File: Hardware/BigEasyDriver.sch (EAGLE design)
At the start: 52 parts, among them IC1 A4983ALT1, IC2 LM317L

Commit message: Started v15 revisions
Changed caps and resis to 0603, updated version number on PCB and
Schematic, re-routed a few traces.  Nowhere near done
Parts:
- C1, C10, C11, C2, C6, C7, C8, C9: device SparkFun:CAP0402-CAP -> SparkFun:CAP0603-CAP
- R1, R10, R11, R12, R13, R2, R20, R3, R4, R5, R6, R7, R8, R9: device SparkFun:RESISTOR0402-RES -> SparkFun:RESISTOR0603-RES
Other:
- note added: "v15"

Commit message: Changed Schematic Nets
Nets changed to new specifications
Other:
- note added: "Revised by Patrick Alberts"
- moved on the sheet: JP10, JP14, JP3, JP6

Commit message: Revert "Changed Schematic Nets"
This reverts commit ceb7b9bd87dc9e1a8942882cf4505f035ac33b39.
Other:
- note removed: "Revised by Patrick Alberts"
- moved on the sheet: JP10, JP14, JP3, JP6

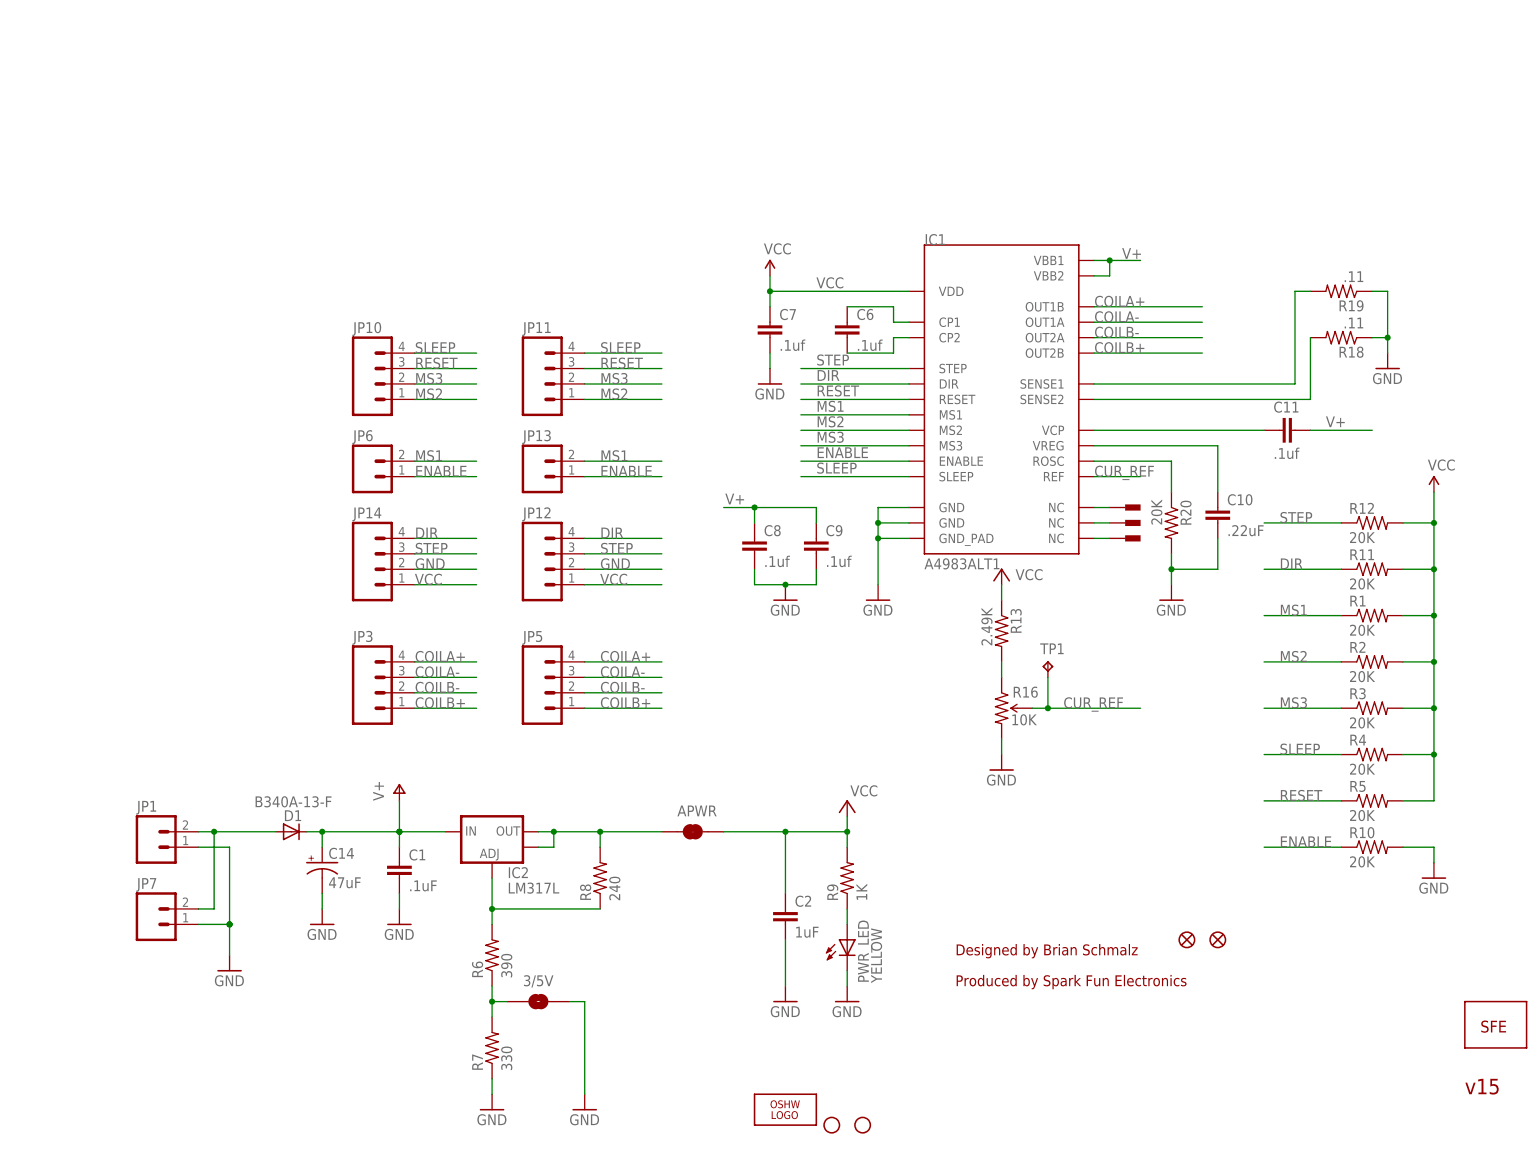
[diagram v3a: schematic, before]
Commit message: Updated Schematic
Changed the nets, the previous commit did not sync correctly.
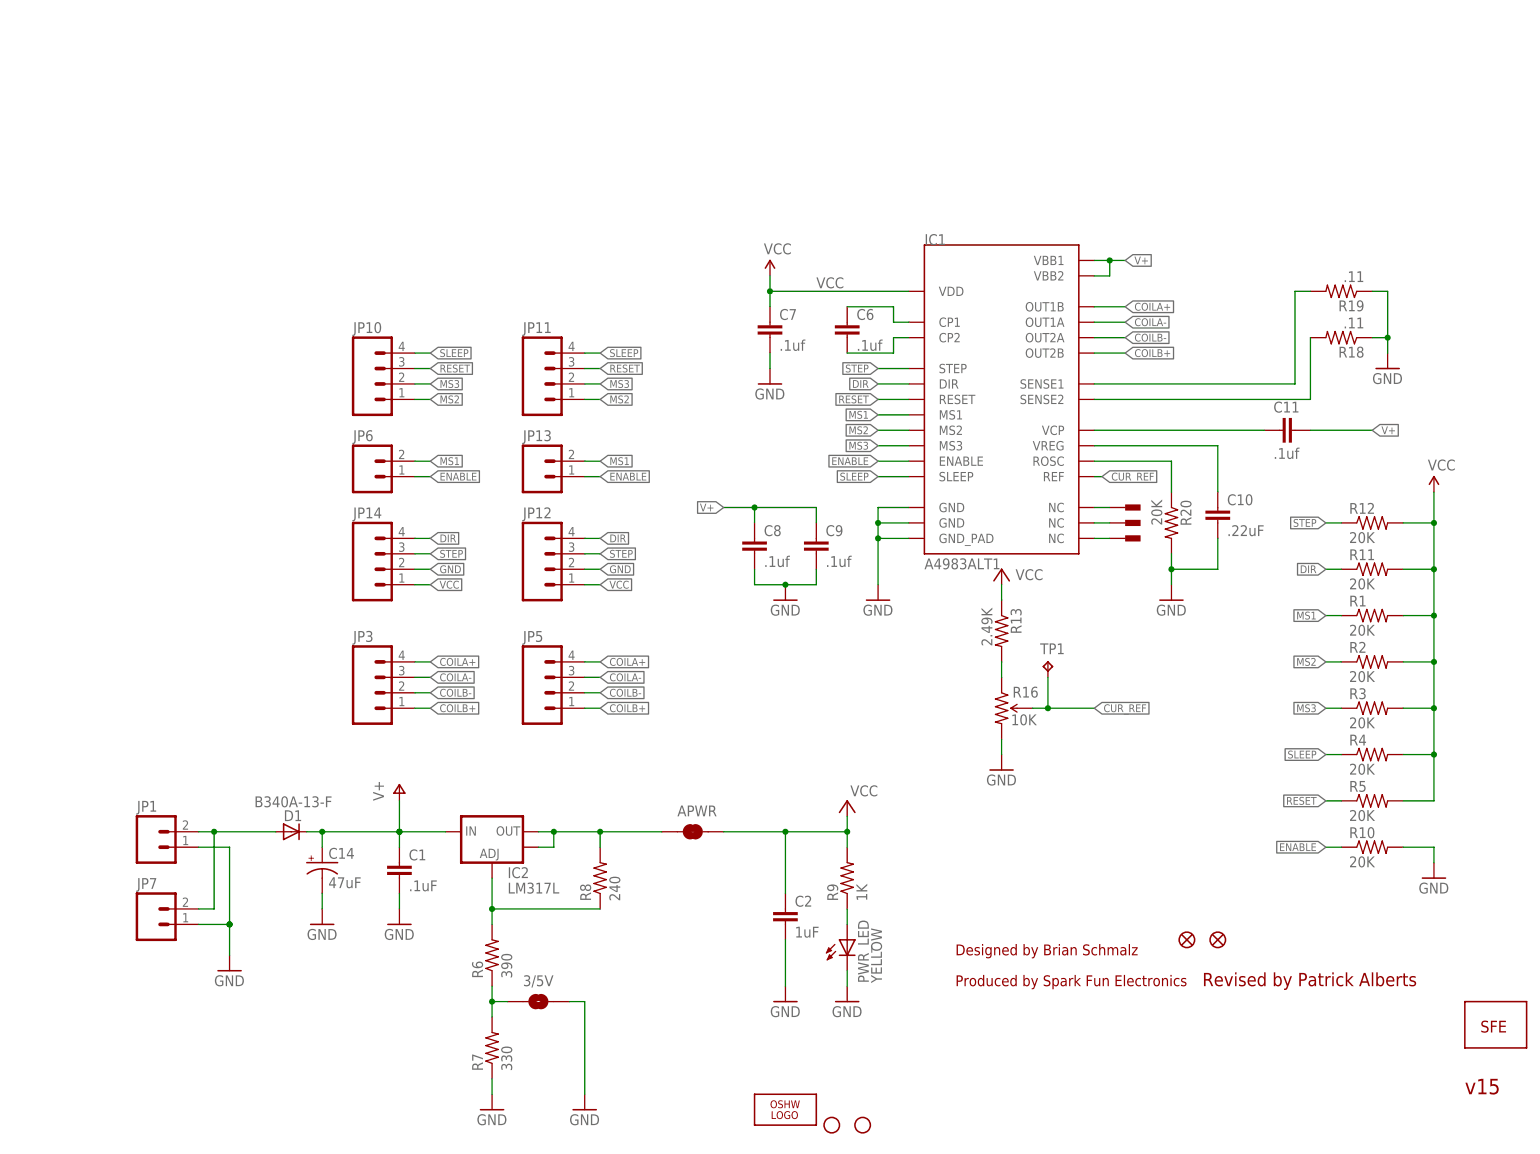
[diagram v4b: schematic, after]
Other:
- note added: "Revised by Patrick Alberts"

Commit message: Frame updated, Angles , Creative Commons added
Added new schematic framrs, cleaned up some trace angels and added the
creative commons license.
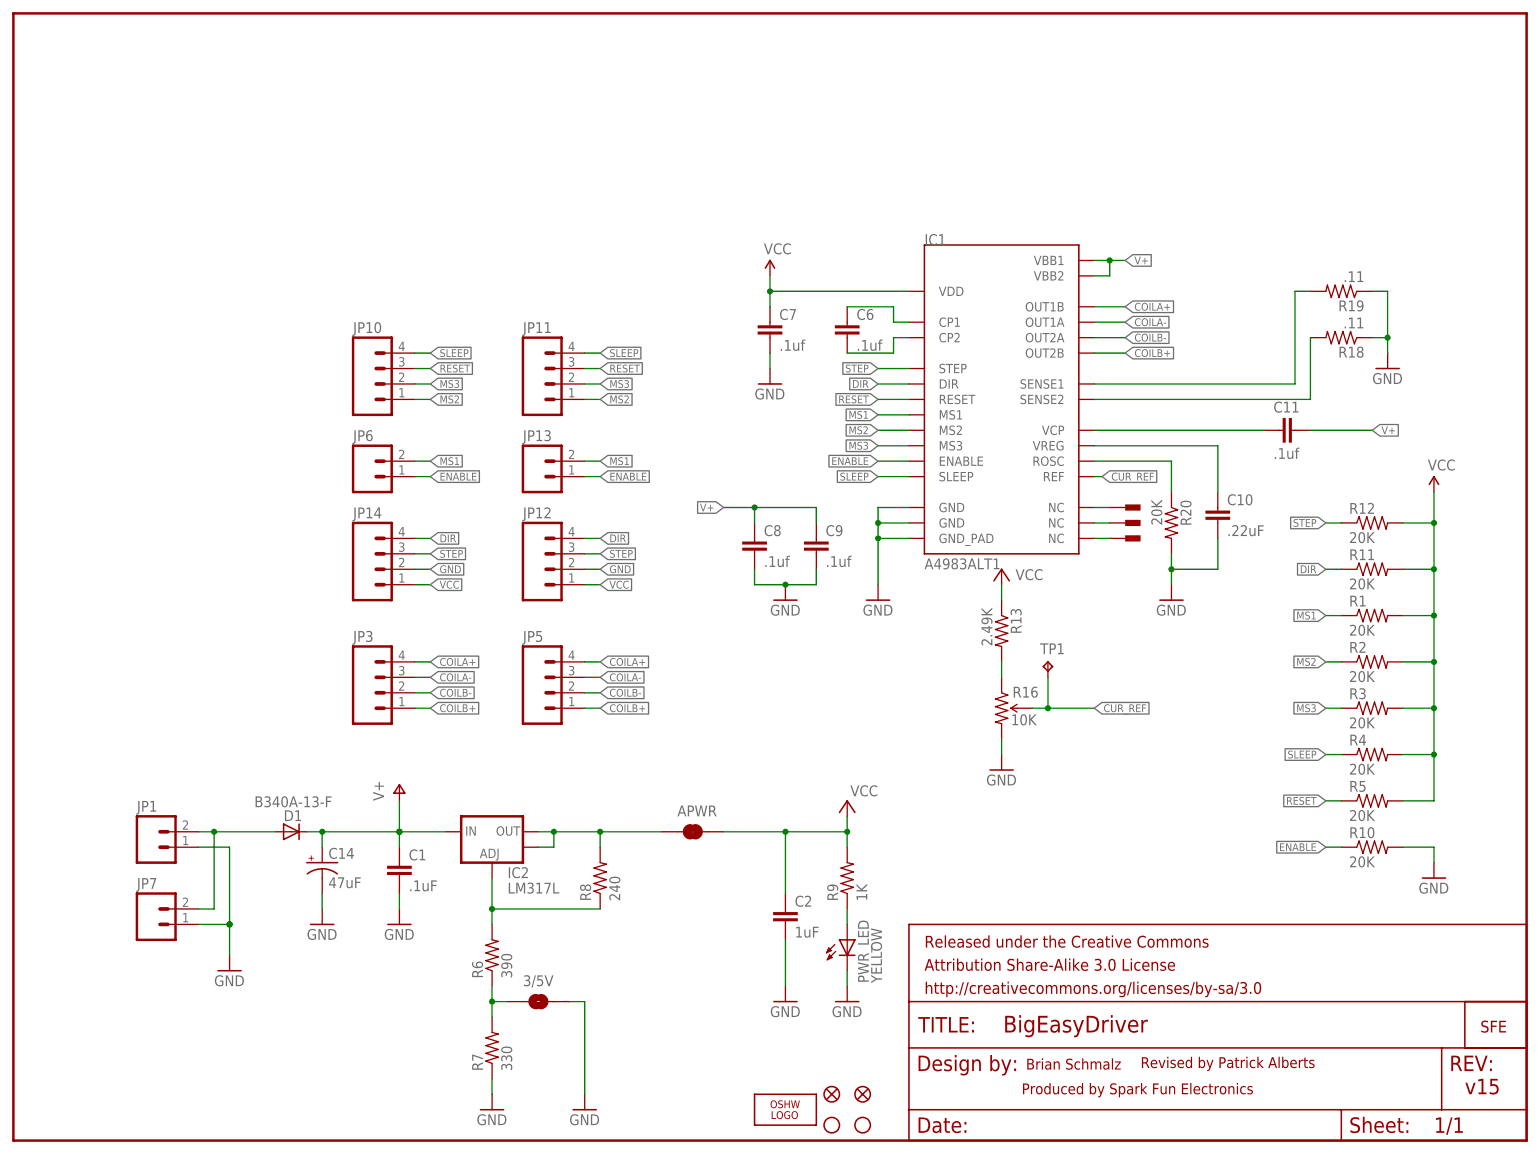
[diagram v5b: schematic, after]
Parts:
- added FRAME1: FRAME-LETTER, SparkFun-Aesthetics:FRAME-LETTER
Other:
- note added: "Brian Schmalz"
- note removed: "Designed by Brian Schmalz"
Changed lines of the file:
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@@
 <layer number="144" name="DrillLegend" color="7" fill="1" visible="no" active="yes"/>
 <layer number="151" name="HeatSink" color="7" fill="1" visible="yes" active="yes"/>
+<layer number="199" name="Contour" color="7" fill="1" visible="no" active="yes"/>
 <layer number="200" name="200bmp" color="1" fill="10" visible="no" active="no"/>
 <layer number="201" name="201bmp" color="2" fill="1" visible="no" active="no"/>
@@
 <part name="MOT_PWR" library="supply1" deviceset="V+" device=""/>
 <part name="GND1" library="supply1" deviceset="GND" device=""/>
-<part name="FRAME1" library="SparkFun" deviceset="FRAME-LETTER" device=""/>
+<part name="FRAME1" library="SparkFun-Aesthetics" deviceset="FRAME-LETTER" device=""/>
 <part name="R6" library="SparkFun" deviceset="RESISTOR" device="0603-RES" value="390"/>
 <part name="R8" library="SparkFun" deviceset="RESISTOR" device="0603-RES" value="240"/>
@@
 <wire x1="12.7" y1="30.48" x2="12.7" y2="55.88" width="0.1524" layer="98" style="shortdash"/>
 <wire x1="111.252" y1="50.8" x2="112.268" y2="50.8" width="0.1524" layer="94"/>
-<text x="154.94" y="30.48" size="1.778" layer="94">Designed by Brian Schmalz</text>
-<text x="154.94" y="25.4" size="1.778" layer="94">Produced by Spark Fun Electronics</text>
+<text x="165.862" y="11.684" size="1.778" layer="94"> Brian Schmalz</text>
+<text x="165.862" y="7.62" size="1.778" layer="94">Produced by Spark Fun Electronics</text>
 <text x="142.24" y="53.34" size="1.778" layer="98">Voltage regulator can supply 100mA</text>
 <text x="71.12" y="58.42" size="1.778" layer="98">Must use LM317</text>
@@
 <text x="2.54" y="2.54" size="1.778" layer="98">-moved vias and retraced as necessary on VCC and TOP layers</text>
 <text x="238.76" y="7.62" size="2.54" layer="94" font="vector">v15</text>
-<text x="195.58" y="25.4" size="2.1844" layer="94" font="vector">Revised by Patrick Alberts</text>
+<text x="185.42" y="11.938" size="1.778" layer="94">Revised by Patrick Alberts</text>
 </plain>
 <instances>
@@
 <instance part="C2" gate="G$1" x="127" y="35.56"/>
 <instance part="LOGO1" gate="G$1" x="127" y="5.08"/>
-<instance part="JP2" gate="G$1" x="193.04" y="33.02"/>
-<instance part="JP4" gate="G$1" x="198.12" y="33.02"/>
+<instance part="JP2" gate="G$1" x="139.7" y="7.62"/>
+<instance part="JP4" gate="G$1" x="134.62" y="7.62"/>
 <instance part="U$3" gate="G$1" x="185.42" y="104.14"/>
 <instance part="U$4" gate="G$1" x="185.42" y="101.6"/>
@@
 <wire x1="124.46" y1="142.24" x2="124.46" y2="139.7" width="0.1524" layer="91"/>
 <junction x="124.46" y="139.7"/>
-<label x="132.08" y="140.208" size="1.778" layer="95"/>
 <pinref part="IC1" gate="G$1" pin="VDD"/>
 <pinref part="C7" gate="G$1" pin="1"/>

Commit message: Version 1.6 update -
* Removed large hole on bottom solder mask (because vias will short out with plane if a metal heatsink is used, this is kinda pointless)
* Changed R13 to 8.3K to give much more useful range of pot motion
* Added current limiting resistors to STEP and DIR lines
* got rid of all angle errors in DRC
* Added more explanation of R16 current adjust pot behavior in schematic
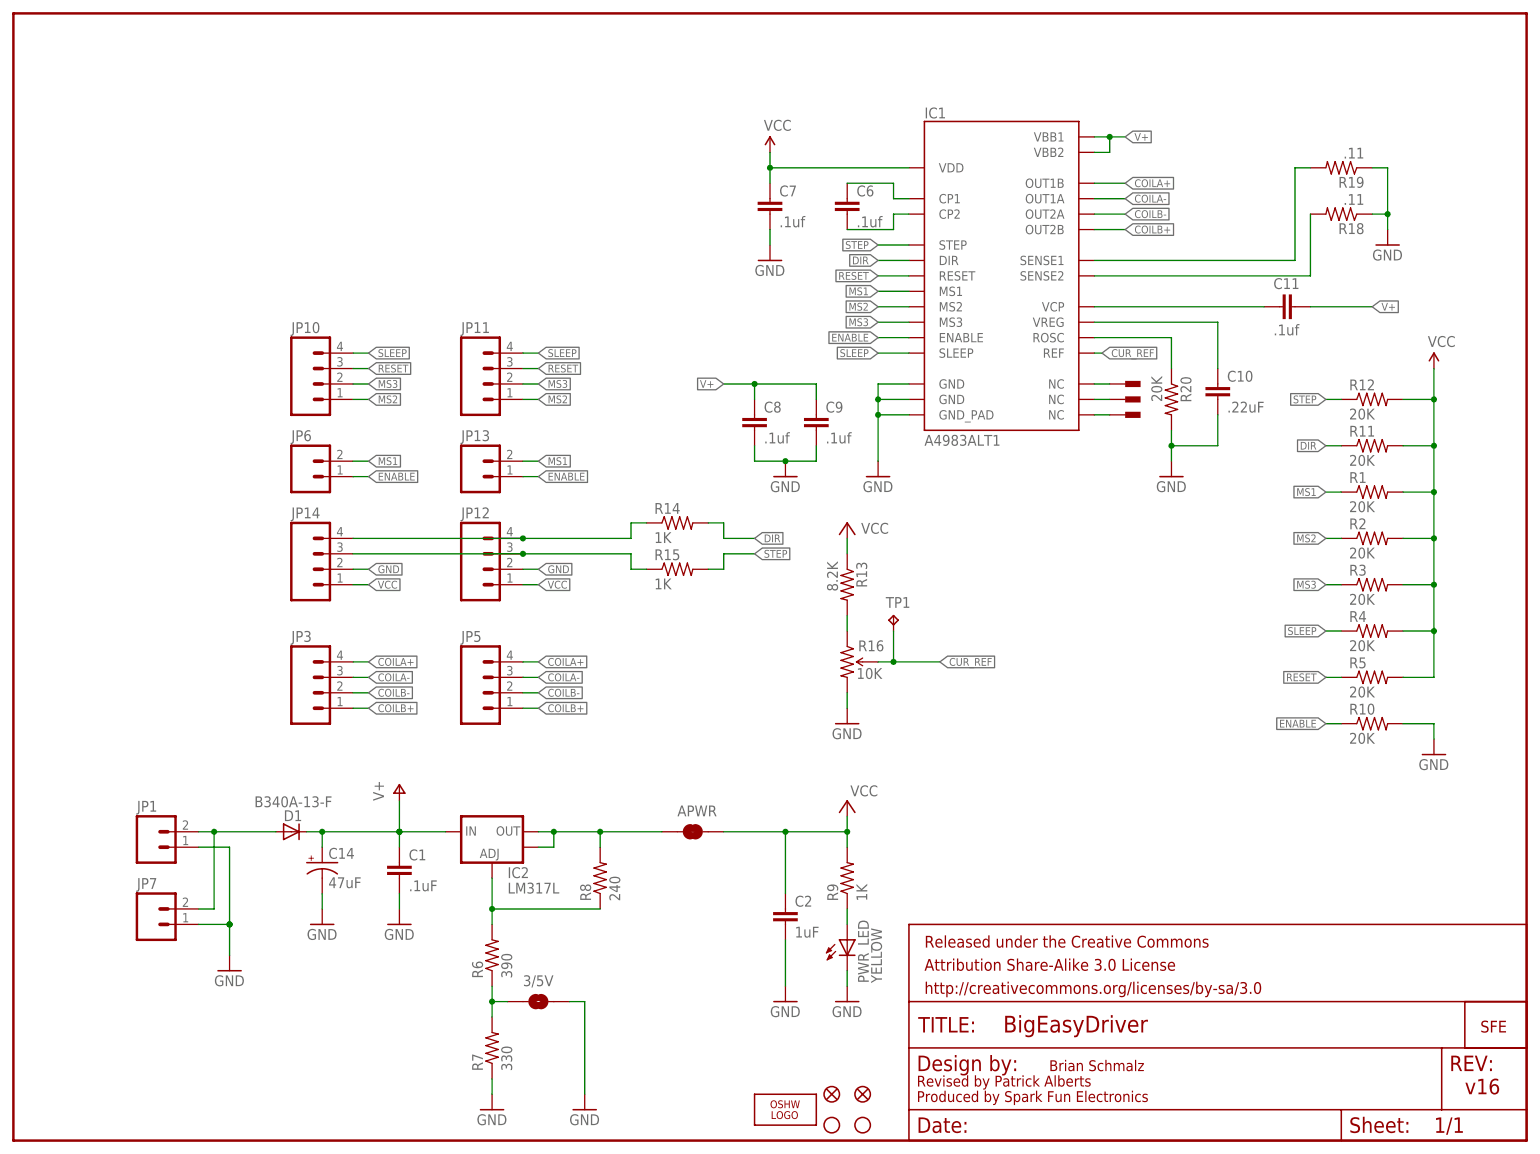
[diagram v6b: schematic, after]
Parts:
- added R14, R15: 1K, SparkFun:RESISTOR0603-RES
- R13: value 2.49K -> 8.2K
- R16: device SparkFun:TRIMPOTSMD -> SparkFun-Electromechanical:TRIMPOT3MM-2
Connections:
- new net N$55: JP12.4, JP14.4, R14.1
- new net N$56: JP12.3, JP14.3, R15.1
- net DIR: now also R14.2; no longer JP12.4, JP14.4
- net STEP: now also R15.2; no longer JP12.3, JP14.3
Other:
- note added: "Added current limiting resistors to STEP and DIR"
- note added: "BigEasyDriver v1.6"
- note added: "Changed R13 to 8.2K to improve range of current adjust pot"
- note added: "Changed license from CC by 3.0 to CC by-sa 3.0"
- note added: "Current adjust pot: adjusts max coil current. R13 set such that: At VCC = 3.3V, full clockwise = 2.08A coil current At VCC = 5V, 64% clockwise = 2.0A coil current Note driver can only output 2A coil current, and is dependent on input voltage, motor, and heat sinking/fan to reach this."
- note added: "Removed large hole in solder mask on bottom"
- note added: "SparkFun design rules applied - minor layout tweaks, R13 now 2.49K"
- note added: "Updated to standard 0603 foorprints, some rerouting, schematic nets changed"
- note added: "You only need to connect M+, GND, STEP, DIR and the motor outputs. All other I/O is set to default to 1/16th microstep mode, and connections are not required for basic operation."
- note added: "v1.0 BPS Origonal version"
- note added: "v1.1 BPS Added pull-ups, re-routed"
- note added: "v1.2 5/2/11 BPS Silk screen corrections, sense resistors now .11 ohms"
- note added: "v1.3 SF 1/10/12"
- note added: "v1.4 SF 4/17/2013 Fixed current adjustment pot silk so directions are correct"
- note added: "v1.5 SF 6/27/2013"
- note added: "v1.6 BPS 3/28/2014"
- note added: "v16"
- note removed: "1/10/12 -v13- Changes:"
- note removed: "All other I/O is set to default"
- note removed: "Attribution 3.0 US License"
- note removed: "BigEasyDriver v1.2"
- note removed: "BigEasyDriver v1.2 by Brian Schmalz is"
- note removed: "Current adj pot"
- note removed: "Motor current 0mA to 2.4A"
- note removed: "STEP, DIR and the motor outputs"
- note removed: "SparkFun design rules applied - minor layout tweaks, R13 now XXX"
- note removed: "You only need to connect M+, GND"
- note removed: "licensed under a Creative Commons"
- note removed: "to 1/16th microstep mode"
- note removed: "v1.0 Origonal version"
- note removed: "v1.1 Added pull-ups, re-routed"
- note removed: "v1.2 5/2/11 Silk screen corrections, sense resistors now .11 ohms"
- note removed: "v15"
- moved on the sheet: C10, C11, C6, C7, C8, C9, IC1, JP10, JP11, JP12, JP13, JP14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
